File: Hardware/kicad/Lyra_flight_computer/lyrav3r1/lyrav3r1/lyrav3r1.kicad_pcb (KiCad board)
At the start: 4 copper layers, 25 x 55 mm, 106 parts, among them IC1 TESEO-LIV3F, J1 Conn_01x02, J2 Screw_Terminal_01x06, J3 Conn_Coaxial, J4 Conn_01x02, J7 USB_B_Micro, J9 Screw_Terminal_01x06, Q1 AO3401A, Q2 AO3400A, Q3 AO3400A, Q4 AO3400A, Q5 AO3400A, U1 SX1262, U2 BMI088, U3 BMP388, U4 ADXL375BCCZ-RL7, U5 M3406, U6 SKY13453-385LF, U7 WS7916S-6/TR, U8 RP2040, U9 W25Q128JVS, X2 SX1M12.000M10F30TNN, Y1 CF4032M00012001

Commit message: w45dytfv
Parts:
- removed R13, R24, R25: 5.1k, Resistor_SMD:R_0402_1005Metric
- removed R16, R26, R27: 1k, Resistor_SMD:R_0402_1005Metric
- removed R21, R23: 15k, Resistor_SMD:R_0402_1005Metric
- added AE1: Antenna, APAE1575R1820ABDC1_T:XDCR_APAE1575R1820ABDC1-T, F.Cu at (196.0, 79.5)
- added J5: Conn_01x05, .pretty:Pad_01x_05, F.Cu at (175.3, 80.8)
- added Q10: AO3400A, Package_TO_SOT_SMD:SOT-23, B.Cu at (195.8, 98.7)
- added Q7: AO3400A, Package_TO_SOT_SMD:SOT-23, B.Cu at (206.6, 98.3)
- added Q8: AO3400A, Package_TO_SOT_SMD:SOT-23, B.Cu at (206.4, 108.4)
- added Q9: AO3400A, Package_TO_SOT_SMD:SOT-23, B.Cu at (195.8, 102.3)
- C23, J7, Q2, Q3, Q4, Q5, U1, U5, U7, Y1: moved to B.Cu
- R10, R11: value 15k -> 1k; moved to B.Cu
- R12: value 5.1k -> 1k; moved to B.Cu
- TP1: footprint TestPoint:TestPoint_Keystone_5019_Minature -> TestPoint:TestPoint_Pad_1.0x1.0mm
- moved Q3 91.3 mm to (206.4, 103.6)
- moved Q2 88.6 mm to (202.7, 103.5), turned to -90 degrees
- moved Q5 87.0 mm to (202.7, 108.4), turned to -90 degrees
- moved Q4 86.6 mm to (202.9, 98.3), turned to -90 degrees
- moved R11 83.1 mm to (202.6, 106.0), turned to 180 degrees
- moved R10 82.3 mm to (202.7, 101.1), turned to 180 degrees
- moved R12 75.5 mm to (195.7, 104.7)
- moved U5 56.5 mm to (185.7, 101.2), turned to 180 degrees
- moved U1 54.4 mm to (187.8, 109.8), turned to 90 degrees
- moved J3 50.9 mm to (196.1, 117.0), turned to 180 degrees
- moved C5 38.4 mm to (214.2, 115.8)
- moved C6 38.4 mm to (214.2, 118.3)
- moved R7 38.4 mm to (213.7, 109.6)
- moved R8 38.4 mm to (213.7, 111.6)
- moved R9 38.4 mm to (213.7, 113.6)
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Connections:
- Q3 pad 1: /P1 EN  -> /P2-
- Q3 pad 3: /P1- -> /P2 CONT 
- Q4 pad 1: /P3 EN  -> /P1 EN 
- Q4 pad 3: /P3- -> /P1-
- Q5 pad 1: /P4 EN  -> /P3 EN 
- Q5 pad 3: /P4- -> /P3-
- R10 pad 1: /P1- -> GND
- R10 pad 2: /P1 CONT  -> /P2 EN 
- R11 pad 1: /P3- -> GND
- R11 pad 2: /P3 CONT  -> /P3 EN 
- R12 pad 1: /P1 CONT  -> GND
- R12 pad 2: GND -> /P4 EN 
- R17 pad 2: /P3 EN  -> /P1 EN 

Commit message: asd
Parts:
- added FL1: SAFEA1G58KA0F00R15, .pretty:FILTER-SMD_5P-L1.4-W1.1-L, F.Cu at (222.9, 91.8)
- moved U1 0.56 mm to (188.1, 110.2)
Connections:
- net +12V renamed /BATT POSTSW
- C5 pad 1: +12P -> +BATT
- C7 pad 1: +12P -> +BATT
- C8 pad 1: +12P -> +BATT
- C9 pad 1: +12P -> +BATT
- J2 pad 2: +12P -> +BATT
- J2 pad 4: +BATT -> /BATT RAW
- J2 pad 6: +BATT -> /BATT RAW
- J9 pad 1: +12P -> +BATT
- J9 pad 3: +12P -> +BATT
- J9 pad 5: +12P -> +BATT
- Q1 pad 2: +12P -> +BATT
- R4 pad 1: +12P -> +BATT
- U5 pad 1: +12P -> +BATT
- U5 pad 4: +12P -> +BATT
- U7 pad 6: /ANT -> Net-(FL1-IN)

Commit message: work
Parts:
- added C32: 120p, Capacitor_SMD:C_0402_1005Metric, F.Cu at (213.0, 86.4)
- FL1, U3, U4: moved to B.Cu
- moved FB2 89.4 mm to (216.1, 142.1)
- moved L4 89.4 mm to (190.4, 149.1)
- moved L5 89.4 mm to (198.9, 132.8)
- moved L8 89.4 mm to (198.9, 138.8)
- moved C29 89.4 mm to (201.7, 132.8)
- moved C30 89.4 mm to (201.7, 134.8)
- moved C31 89.4 mm to (201.7, 136.8)
- moved C35 89.4 mm to (201.7, 138.7)
- moved C36 89.4 mm to (201.7, 140.7)
- moved C37 89.4 mm to (201.7, 142.7)
- moved C38 89.4 mm to (204.6, 132.8)
- moved C39 89.4 mm to (204.6, 134.8)
- moved C40 89.4 mm to (204.6, 136.8)
- moved C41 89.4 mm to (204.6, 138.7)
- moved C42 89.4 mm to (204.6, 140.7)
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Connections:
- U8 pad 15: unconnected-(U8-GPIO12-Pad15) -> /MISO
- U8 pad 17: unconnected-(U8-GPIO14-Pad17) -> /SCK
- U8 pad 18: unconnected-(U8-GPIO15-Pad18) -> /MOSI
- U8 pad 2: /P3 CONT  -> unconnected-(U8-GPIO0-Pad2)
- U8 pad 28: unconnected-(U8-GPIO17-Pad28) -> /SX CS
- U8 pad 29: unconnected-(U8-GPIO18-Pad29) -> /P3 CONT 
- U8 pad 3: /P3 EN  -> unconnected-(U8-GPIO1-Pad3)
- U8 pad 30: unconnected-(U8-GPIO19-Pad30) -> /P3 EN 
- U8 pad 31: unconnected-(U8-GPIO20-Pad31) -> /P2 CONT 
- U8 pad 32: /BUZZER -> /P2 EN 
- U8 pad 34: unconnected-(U8-GPIO22-Pad34) -> /P1 CONT 
- U8 pad 35: unconnected-(U8-GPIO23-Pad35) -> /P1 EN 
- U8 pad 36: unconnected-(U8-GPIO24-Pad36) -> /P4 CONT 
- U8 pad 37: /BRKOUT1 -> /P4 EN 
- U8 pad 4: /P2 CONT  -> unconnected-(U8-GPIO2-Pad4)
- U8 pad 5: /P2 EN  -> unconnected-(U8-GPIO3-Pad5)
- U8 pad 6: /P1 CONT  -> unconnected-(U8-GPIO4-Pad6)
- U8 pad 7: /P1 EN  -> unconnected-(U8-GPIO5-Pad7)
- U8 pad 8: /P4 CONT  -> unconnected-(U8-GPIO6-Pad8)
- U8 pad 9: /P4 EN  -> unconnected-(U8-GPIO7-Pad9)

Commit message: redoing stuff
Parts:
- removed C10: 1u, Capacitor_SMD:C_0402_1005Metric
- removed C11: 100n, Capacitor_SMD:C_0402_1005Metric
- removed J9: Screw_Terminal_01x06, TerminalBlock_Phoenix:TerminalBlock_Phoenix_MPT-0,5-6-2.54_1x06_P2.54mm_Horizontal
- removed R2, R22, R9: 1k, Resistor_SMD:R_0402_1005Metric
- removed U4: ADXL375BCCZ-RL7, easyeda2kicad:LGA-14_L5.0-W3.0-P0.80-BL
- added BZ1: Buzzer, .pretty:Buzzer_12x9.5RM7.6, F.Cu at (202.1, 96.5)
- added C14: 10u, Capacitor_SMD:C_0603_1608Metric, F.Cu at (166.4, 50.0)
- added C15: 1n, Capacitor_SMD:C_0402_1005Metric, F.Cu at (169.8, 51.7)
- added C20: 56p, Capacitor_SMD:C_0603_1608Metric, F.Cu at (166.4, 52.6)
- added C28: 1n, Capacitor_SMD:C_0402_1005Metric, F.Cu at (169.8, 53.7)
- added C33: 1n, Capacitor_SMD:C_0402_1005Metric, B.Cu at (196.8, 81.1)
- added C34: 10u, Capacitor_SMD:C_0603_1608Metric, F.Cu at (166.4, 55.1)
- added C50: 100n, Capacitor_SMD:C_0402_1005Metric, F.Cu at (221.3, 97.4)
- added D3: LED, LED_SMD:LED_0805_2012Metric, F.Cu at (166.6, 66.4)
- added J8: Screw_Terminal_01x07, TerminalBlock_Phoenix:TerminalBlock_Phoenix_MPT-0,5-7-2.54_1x07_P2.54mm_Horizontal, F.Cu at (188.5, 108.8)
- added L2: 4.7u, Inductor_SMD:L_Changjiang_FNR3015S, B.Cu at (202.9, 101.4)
- added R13: 5.1k, Resistor_SMD:R_0402_1005Metric, F.Cu at (152.1, 65.5)
- added R16: 5.1k, Resistor_SMD:R_0402_1005Metric, F.Cu at (152.1, 67.5)
- added TP2: TestPoint, TestPoint:TestPoint_Pad_1.0x1.0mm, F.Cu at (207.6, 85.0)
- added TP3: TestPoint, TestPoint:TestPoint_Pad_1.0x1.0mm, B.Cu at (207.6, 85.0)
- added U10: MT2492, .pretty:SOT-23-6_L2.9-W1.6-P0.95-LS2.8-BL, B.Cu at (199.3, 101.5)
- C29, C30, C31, C35, C36, C37, C38, C39, C40, C41, C42, C43, C44, C45, C46, C47, C48, C49, FB2, L4, L5, L6, L7, L8, L9, Q1, R17, R19, R6, U6, X2: moved to B.Cu
- C32: value 120p -> 1u
- C5: value 4u7 -> 22u; footprint Capacitor_SMD:C_0603_1608Metric -> Capacitor_SMD:C_0805_2012Metric; moved to B.Cu
- C6: value 10u -> 22nf; footprint Capacitor_SMD:C_0603_1608Metric -> Capacitor_SMD:C_0402_1005Metric; moved to B.Cu
- C9: value 680uf -> 22u; footprint Capacitor_THT:CP_Radial_D6.3mm_P2.50mm -> Capacitor_SMD:C_0805_2012Metric; moved to B.Cu
- J2: value Screw_Terminal_01x06 -> Screw_Terminal_01x02; footprint TerminalBlock_Phoenix:TerminalBlock_Phoenix_MPT-0,5-6-2.54_1x06_P2.54mm_Horizontal -> TerminalBlock_Phoenix:TerminalBlock_Phoenix_MPT-0,5-2-2.54_1x02_P2.54mm_Horizontal
- R4: value 15k -> 40k
- R5: value 5.1k -> 25k
- R7: value 15k -> 110k; footprint Resistor_SMD:R_0402_1005Metric -> Resistor_SMD:R_0603_1608Metric; moved to B.Cu
- R8: value 50k -> 20k; moved to B.Cu
- U5: value M3406 -> ADXL375BCCZ-RL7; footprint .pretty:SOT-23-5_L3.0-W1.7-P0.95-LS2.8-BR -> easyeda2kicad:LGA-14_L5.0-W3.0-P0.80-BL
- moved C4 101.1 mm to (221.3, 91.4)
- moved C12 98.1 mm to (221.3, 93.4)
- moved R17 82.5 mm to (200.8, 114.6)
- moved U6 81.7 mm to (193.4, 70.1), turned to 180 degrees
- moved Q1 80.2 mm to (193.4, 101.2), turned to 180 degrees
- moved L4 75.6 mm to (184.4, 73.7), turned to -90 degrees
- moved L5 75.5 mm to (230.0, 64.0), turned to 180 degrees
- moved L6 75.5 mm to (230.0, 66.0), turned to 180 degrees
- moved R19 74.2 mm to (191.4, 68.9)
- moved C29 73.3 mm to (227.1, 64.0), turned to 180 degrees
- moved C31 73.3 mm to (227.1, 68.0), turned to 180 degrees
- moved C36 73.3 mm to (227.1, 71.9), turned to 180 degrees
- moved C37 73.3 mm to (227.1, 73.9), turned to 180 degrees
- moved C49 72.1 mm to (191.1, 76.9)
- moved C43 72.1 mm to (193.6, 71.4)
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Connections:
- C32 pad 1: Net-(FL1-OUT) -> +3V3
- C32 pad 2: /ANT -> GND
- C6 pad 1: +3V3 -> Net-(U10-BS)
- C6 pad 2: GND -> Net-(U10-SW)
- C9 pad 1: +BATT -> +3V3
- IC1 pad 10: /RF GND 1 -> GND
- IC1 pad 12: /RF GND 2 -> GND
- IC1 pad 4: /PPS -> Net-(IC1-1PPS)
- J2 pad 1: /P4- -> /BATT POSTSW
- J2 pad 2: +BATT -> /BATT RAW
- R28 pad 1: /LEDBLUE -> /LEDINDICATION
- R7 pad 1: Net-(U5-SW) -> +3V3
- R7 pad 2: Net-(U5-FB) -> Net-(U10-FB)
- R8 pad 1: Net-(U5-FB) -> Net-(U10-FB)
- U2 pad 10: unconnected-(U2-SDO2-Pad10) -> GND
- U2 pad 14: unconnected-(U2-CSB1-Pad14) -> +3V3
- U2 pad 15: unconnected-(U2-SDO1-Pad15) -> GND
- U2 pad 7: unconnected-(U2-PS-Pad7) -> +3V3
- U2 pad 8: unconnected-(U2-SCL/SCK-Pad8) -> /SCL
- U2 pad 9: unconnected-(U2-SDA/SDI-Pad9) -> /SDA
- U3 pad 2: unconnected-(U3-SCK-Pad2) -> /SCL
- U3 pad 4: unconnected-(U3-SDI-Pad4) -> /SDA
- U3 pad 5: unconnected-(U3-SDO-Pad5) -> GND
- U3 pad 6: unconnected-(U3-CSB-Pad6) -> +3V3
- U5 pad 1: +BATT -> +3V3
- U5 pad 3: Net-(U5-SW) -> +3V3
- U5 pad 4: +BATT -> GND
- U5 pad 5: Net-(U5-FB) -> GND
- U8 pad 11: unconnected-(U8-GPIO8-Pad11) -> /DIO1
- U8 pad 12: /LEDBLUE -> unconnected-(U8-GPIO9-Pad12)
- U8 pad 13: /LEDGREEN -> unconnected-(U8-GPIO10-Pad13)
- U8 pad 14: /LEDRED -> /GPS_RST
- U8 pad 15: /MISO -> /SDA
- U8 pad 16: unconnected-(U8-GPIO13-Pad16) -> /SCL
- U8 pad 17: /SCK -> unconnected-(U8-GPIO14-Pad17)
- U8 pad 18: /MOSI -> /BRKOUT1
- U8 pad 28: /SX CS -> /BUZZER
- U8 pad 29: /P3 CONT  -> /P1 EN 
- U8 pad 30: /P3 EN  -> /P1 CONT 
- U8 pad 31: /P2 CONT  -> /P2 EN 
- U8 pad 32: /P2 EN  -> /P2 CONT 
- U8 pad 34: /P1 CONT  -> /P3 EN 
- U8 pad 35: /P1 EN  -> /P3 CONT 
- U8 pad 36: /P4 CONT  -> /P4 EN 
- U8 pad 37: /P4 EN  -> /P4 CONT 
- U8 pad 5: unconnected-(U8-GPIO3-Pad5) -> /MOSI
- U8 pad 6: unconnected-(U8-GPIO4-Pad6) -> /MISO
- U8 pad 7: unconnected-(U8-GPIO5-Pad7) -> /SX CS
- U8 pad 8: unconnected-(U8-GPIO6-Pad8) -> /SCK
- U8 pad 9: unconnected-(U8-GPIO7-Pad9) -> /BUSY

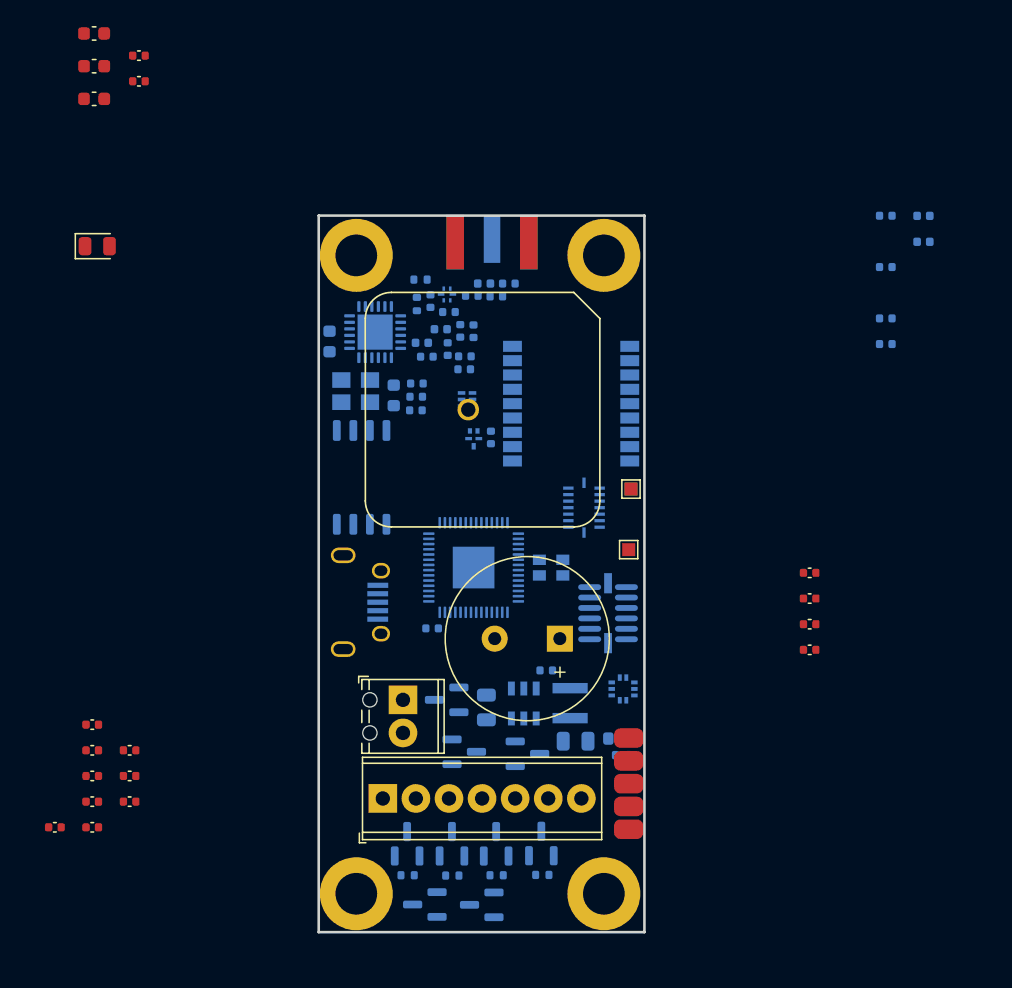
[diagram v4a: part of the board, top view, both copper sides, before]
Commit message: found new gps chip and getting close t oend of schematic
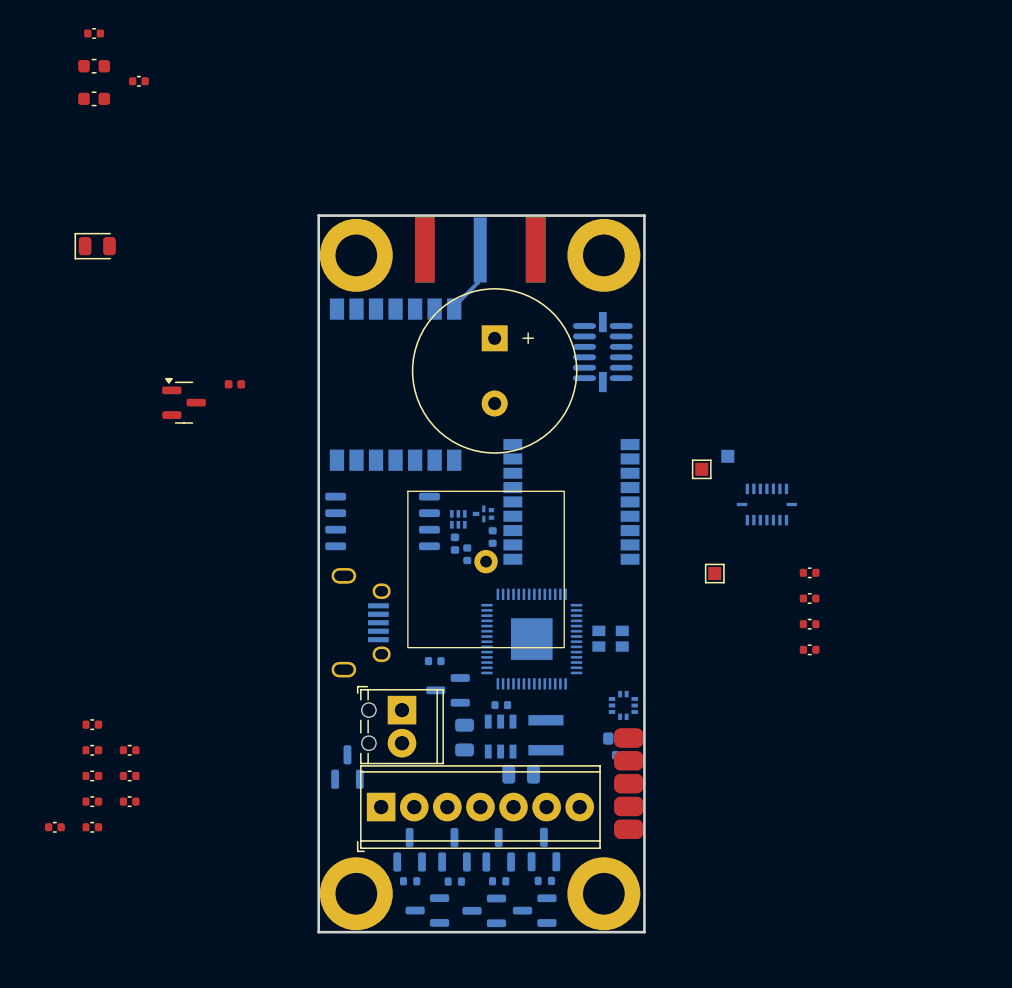
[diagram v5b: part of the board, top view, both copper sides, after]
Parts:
- removed C29: 470nF, Capacitor_SMD:C_0402_1005Metric
- removed C30, C40: 100pF, Capacitor_SMD:C_0402_1005Metric
- removed C31, C38: 3.3pF, Capacitor_SMD:C_0402_1005Metric
- removed C35: 22nF, Capacitor_SMD:C_0402_1005Metric
- removed C36: 4.7pF, Capacitor_SMD:C_0402_1005Metric
- removed C37: 1pF, Capacitor_SMD:C_0402_1005Metric
- removed C39: 18pF, Capacitor_SMD:C_0402_1005Metric
- removed C41: 15pF, Capacitor_SMD:C_0402_1005Metric
- removed C42, C43, C47, C48, C49: 100nF, Capacitor_SMD:C_0402_1005Metric
- removed C44: 33pF, Capacitor_SMD:C_0402_1005Metric
- removed C45, C46: TBD, Capacitor_SMD:C_0402_1005Metric
- removed FB2: 200mA, Inductor_SMD:L_0603_1608Metric
- removed J3: Conn_Coaxial, Connector_Coaxial:SMA_Samtec_SMA-J-P-X-ST-EM1_EdgeMount
- removed L5: 33nH, Inductor_SMD:L_0402_1005Metric
- removed L6: 68nH, Inductor_SMD:L_0402_1005Metric
- removed L7: 3.9nH, Inductor_SMD:L_0402_1005Metric
- removed L8: 15nH, Inductor_SMD:L_0402_1005Metric
- removed L9: 0R, Inductor_SMD:L_0402_1005Metric
- removed R19: 100R, Resistor_SMD:R_0402_1005Metric
- removed R6: 5.1k, Resistor_SMD:R_0402_1005Metric
- removed U1: SX1262, Package_DFN_QFN:QFN-24-1EP_4x4mm_P0.5mm_EP2.7x2.7mm
- removed U6: SKY13453-385LF, .pretty:QFN-6_L1.0-W1.0-P0.50-LS1.0-BL
- removed Y1: CF4032M00012001, Crystal:Crystal_SMD_3225-4Pin_3.2x2.5mm
- added AE2: Antenna, .pretty:SMA-SMD_HJ-SMA086, B.Cu at (196.0, 66.7)
- added L1: 10n, Inductor_SMD:L_0402_1005Metric, F.Cu at (177.2, 77.0)
- added Q11: Q_NPN_BEC, Package_TO_SOT_SMD:SOT-23, F.Cu at (173.3, 78.4)
- added U4: VGDD79S868N0S1, .pretty:WIRELM-SMD_L11.5-W11.5-P1.50-BL, B.Cu at (189.5, 77.0)
- AE1: footprint APAE1575R1820ABDC1_T:XDCR_APAE1575R1820ABDC1-T -> .pretty:APAE1575R1240ABDD1-T
- C14: value 10u -> 10n; footprint Capacitor_SMD:C_0603_1608Metric -> Capacitor_SMD:C_0402_1005Metric
- C15: moved to B.Cu
- C34: value 10u -> 56p
- L4: value 15uH -> 10n; footprint Inductor_SMD:L_0603_1608Metric -> Inductor_SMD:L_0402_1005Metric
- moved C15 45.8 mm to (195.0, 90.0), turned to 90 degrees
- moved BZ1 23.6 mm to (197.1, 73.4), turned to -90 degrees
- moved U5 20.0 mm to (205.4, 74.5)
- moved L4 18.3 mm to (194.1, 89.2), turned to 90 degrees
- moved U2 14.0 mm to (218.0, 86.2), turned to 90 degrees
- moved AE1 12.3 mm to (196.4, 91.2), turned to 0 degrees
- moved Q7 12.0 mm to (200.2, 117.4), turned to 180 degrees
- moved U7 9.22 mm to (194.3, 87.3), turned to 180 degrees
- moved Q8 9.04 mm to (185.8, 106.4), turned to 90 degrees
- moved TP3 7.84 mm to (215.0, 82.5)
- moved C33 7.65 mm to (197.0, 88.7)
- moved IC1 7.54 mm to (203.0, 86.0)
- moved X2 7.11 mm to (206.0, 96.5)
- moved U8 7.08 mm to (200.0, 96.5)
- moved TP1 6.86 mm to (214.0, 91.5)
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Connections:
- L4 pad 1: Net-(U1-DCC_SW) -> Net-(C15-Pad2)
- L4 pad 2: Net-(U1-VREG) -> Net-(U7-RFIN)
- U8 pad 17: unconnected-(U8-GPIO14-Pad17) -> /LEDINDICATION
- U8 pad 3: unconnected-(U8-GPIO1-Pad3) -> /DIO3
- U8 pad 4: unconnected-(U8-GPIO2-Pad4) -> /SX RST
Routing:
- net Net-(AE2-A): track 0.00 -> 5.26 mm

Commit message: qwe
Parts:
- removed U4: VGDD79S868N0S1, .pretty:WIRELM-SMD_L11.5-W11.5-P1.50-BL
- added U1: E22-400MM22S, .pretty:WIRELM-SMD_E22-400MM22S, B.Cu at (189.6, 76.5)
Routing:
- net Net-(AE2-A): track 5.26 -> 2.56 mm
